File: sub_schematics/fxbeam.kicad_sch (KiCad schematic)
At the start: 16 parts

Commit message: buck converter changes
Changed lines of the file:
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@@
 		(color 0 0 0 0)
 	)
-	(junction
-		(at 49.53 111.76)
-		(diameter 0)
-		(color 0 0 0 0)
-	)
 	(bus_entry
 		(at 109.22 135.89)
@@
 	(wire
 		(pts
-			(xy 46.99 111.76) (xy 49.53 111.76)
+			(xy 46.99 111.76) (xy 52.07 111.76)
 		)
 		(stroke
@@
 		)
 	)
-	(wire
-		(pts
-			(xy 49.53 111.76) (xy 52.07 111.76)
-		)
-		(stroke
-			(width 0)
-			(type default)
-		)
-	)
 	(bus
 		(pts
@@
 					(unit 1)
 				)
-			)
-		)
-	)
-	(symbol
-		(lib_id "power:GND")
-		(at 49.53 111.76 0)
-		(unit 1)
-		(body_style 1)
-		(exclude_from_sim no)
-		(in_bom yes)
-		(on_board yes)
-		(in_pos_files yes)
-		(dnp no)
-		(fields_autoplaced yes)
-		(property "Reference" "#PWR01"
-			(at 49.53 118.11 0)
-			(hide yes)
-			(show_name no)
-			(do_not_autoplace no)
-			(effects
-				(font
-					(size 1.27 1.27)
-				)
-			)
-		)
-		(property "Value" "GND"
-			(at 49.53 116.84 0)
-			(show_name no)
-			(do_not_autoplace no)
-			(effects
-				(font
-					(size 1.27 1.27)
-				)
-			)
-		)
-		(property "Footprint" ""
-			(at 49.53 111.76 0)
-			(hide yes)
-			(show_name no)
-			(do_not_autoplace no)
-			(effects
-				(font
-					(size 1.27 1.27)
-				)
-			)
-		)
-		(property "Datasheet" ""
-			(at 49.53 111.76 0)
-			(hide yes)
-			(show_name no)
-			(do_not_autoplace no)
-			(effects
-				(font
-					(size 1.27 1.27)
-				)
-			)
-		)
-		(property "Description" "Power symbol creates a global label with name \"GND\" , ground"
-			(at 49.53 111.76 0)
-			(hide yes)
-			(show_name no)
-			(do_not_autoplace no)
-			(effects
-				(font
-					(size 1.27 1.27)
-				)
-			)
-		)
-		(pin "1"
-		)
-		(instances
-			(project "fw16_MCIO8i"
-				(path "/50f5fd03-67f8-43d1-8bfe-dca2cf908bf0/8477da45-41b5-48a1-9c5b-2402988eb1f4"
-					(reference "#PWR01")
-					(unit 1)
-				)

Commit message: buck converter component
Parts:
- removed R1: 1206_R_560112132036, resistors:R_Wurth_WRIS-RSKS-1206_R, symbol resistor:1206_R_560112132036
- added R19: 1206_R_560112132036, resistors:R_Wurth_WRIS-RSKS-1206_R, symbol resistor:1206_R_560112132036
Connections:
- net GND: now also R19.2
- net at IN1.SL2 (ID1): now also R19.1

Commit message: Schematics revamped
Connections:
- net PEX_RST renamed PEX.RST

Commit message: Footprint
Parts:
- removed D3, D6: ES15DLW, fan-diode:SODFL3718X102N, symbol fan-diode:ES15DLW
- removed R10, R7, R8, R9: 1206_R_560112132007, resistors:R_Wurth_WRIS-RSKS-1206_R, symbol resistor:1206_R_560112132007
- removed R19, R2: 1206_R_560112132036, resistors:R_Wurth_WRIS-RSKS-1206_R, symbol resistor:1206_R_560112132036
- added R10, R7, R8, R9: 0402_560112110001, WE_WRIS-RSKS:R_Wurth_WRIS-RSKS-0402, symbol WE_WRIS-RSKS:0402_560112110001
- added R19, R2: 0402_560112110088, WE_WRIS-RSKS:R_Wurth_WRIS-RSKS-0402, symbol WE_WRIS-RSKS:0402_560112110088
- R3, R4, R5, R6: value 1206_R_560112132007 -> 0402_560112110001; footprint resistors:R_Wurth_WRIS-RSKS-1206_R -> WE_WRIS-RSKS:R_Wurth_WRIS-RSKS-0402; symbol resistor:1206_R_560112132007 -> WE_WRIS-RSKS:0402_560112110001; H (mm) 0.6 -> 0.35; L (mm) 3.1 -> 1.0; LCSC Part # C25268462 -> (none); MPN 560112132007 -> (none); PRated (mW) 250.0 -> 62.5; Part Number 560112132007 -> 560112110001; Size 1206_R -> 0402; W (mm) 1.6 -> 0.5
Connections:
- net 12V_PWR: now also R7.2
- net FAN1.PWM: now also R9.2
- net FAN1.SPD: now also R8.2
- net GND: now also R6.2, R10.2, R19.1, R2.1
- net at IN1.SL2 (ID1): now also R2.2
- net at IN1.PJ1 (ID0): now also R19.2
- net at FAN_R1.4: now also R7.1
- net at FAN_R1.1: now also R10.1
- net at FAN_R1.3: now also R8.1
- net at FAN_R1.2: now also R9.1

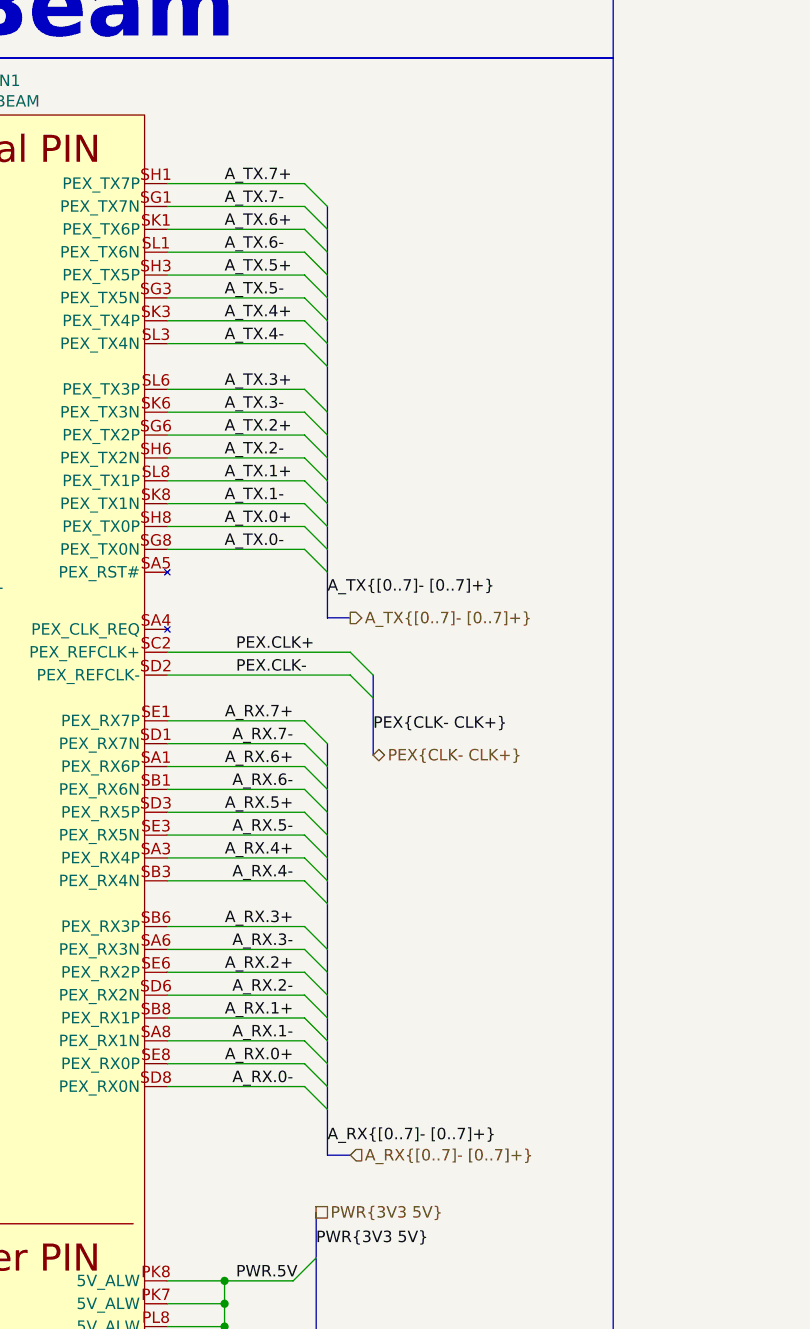
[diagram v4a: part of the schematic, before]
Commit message: PCIe shematic fix
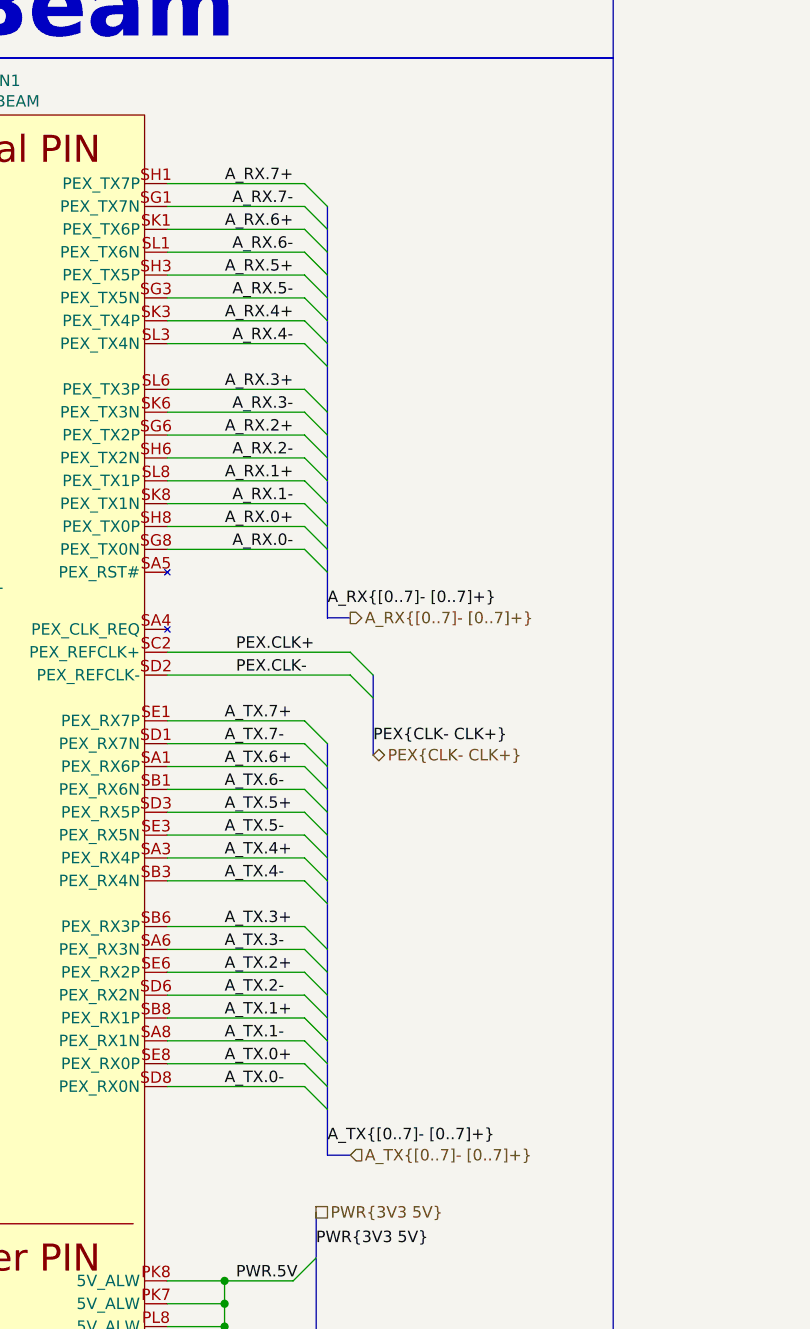
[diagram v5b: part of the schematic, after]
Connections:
- net A_RX.0+: now also IN1.SH8 (PEX_TX0P); no longer IN1.SE8 (PEX_RX0P)
- net A_RX.0-: now also IN1.SG8 (PEX_TX0N); no longer IN1.SD8 (PEX_RX0N)
- net A_RX.1+: now also IN1.SL8 (PEX_TX1P); no longer IN1.SB8 (PEX_RX1P)
- net A_RX.1-: now also IN1.SK8 (PEX_TX1N); no longer IN1.SA8 (PEX_RX1N)
- net A_RX.2+: now also IN1.SG6 (PEX_TX2P); no longer IN1.SE6 (PEX_RX2P)
- net A_RX.2-: now also IN1.SH6 (PEX_TX2N); no longer IN1.SD6 (PEX_RX2N)
- net A_RX.3+: now also IN1.SL6 (PEX_TX3P); no longer IN1.SB6 (PEX_RX3P)
- net A_RX.3-: now also IN1.SK6 (PEX_TX3N); no longer IN1.SA6 (PEX_RX3N)
- net A_RX.4+: now also IN1.SK3 (PEX_TX4P); no longer IN1.SA3 (PEX_RX4P)
- net A_RX.4-: now also IN1.SL3 (PEX_TX4N); no longer IN1.SB3 (PEX_RX4N)
- net A_RX.5+: now also IN1.SH3 (PEX_TX5P); no longer IN1.SD3 (PEX_RX5P)
- net A_RX.5-: now also IN1.SG3 (PEX_TX5N); no longer IN1.SE3 (PEX_RX5N)
- net A_RX.6+: now also IN1.SK1 (PEX_TX6P); no longer IN1.SA1 (PEX_RX6P)
- net A_RX.6-: now also IN1.SL1 (PEX_TX6N); no longer IN1.SB1 (PEX_RX6N)
- net A_RX.7+: now also IN1.SH1 (PEX_TX7P); no longer IN1.SE1 (PEX_RX7P)
- net A_RX.7-: now also IN1.SG1 (PEX_TX7N); no longer IN1.SD1 (PEX_RX7N)
- net A_TX.0+: now also IN1.SE8 (PEX_RX0P); no longer IN1.SH8 (PEX_TX0P)
- net A_TX.0-: now also IN1.SD8 (PEX_RX0N); no longer IN1.SG8 (PEX_TX0N)
- net A_TX.1+: now also IN1.SB8 (PEX_RX1P); no longer IN1.SL8 (PEX_TX1P)
- net A_TX.1-: now also IN1.SA8 (PEX_RX1N); no longer IN1.SK8 (PEX_TX1N)
- net A_TX.2+: now also IN1.SE6 (PEX_RX2P); no longer IN1.SG6 (PEX_TX2P)
- net A_TX.2-: now also IN1.SD6 (PEX_RX2N); no longer IN1.SH6 (PEX_TX2N)
- net A_TX.3+: now also IN1.SB6 (PEX_RX3P); no longer IN1.SL6 (PEX_TX3P)
- net A_TX.3-: now also IN1.SA6 (PEX_RX3N); no longer IN1.SK6 (PEX_TX3N)
- net A_TX.4+: now also IN1.SA3 (PEX_RX4P); no longer IN1.SK3 (PEX_TX4P)
- net A_TX.4-: now also IN1.SB3 (PEX_RX4N); no longer IN1.SL3 (PEX_TX4N)
- net A_TX.5+: now also IN1.SD3 (PEX_RX5P); no longer IN1.SH3 (PEX_TX5P)
- net A_TX.5-: now also IN1.SE3 (PEX_RX5N); no longer IN1.SG3 (PEX_TX5N)
- net A_TX.6+: now also IN1.SA1 (PEX_RX6P); no longer IN1.SK1 (PEX_TX6P)
- net A_TX.6-: now also IN1.SB1 (PEX_RX6N); no longer IN1.SL1 (PEX_TX6N)
- net A_TX.7+: now also IN1.SE1 (PEX_RX7P); no longer IN1.SH1 (PEX_TX7P)
- net A_TX.7-: now also IN1.SD1 (PEX_RX7N); no longer IN1.SG1 (PEX_TX7N)

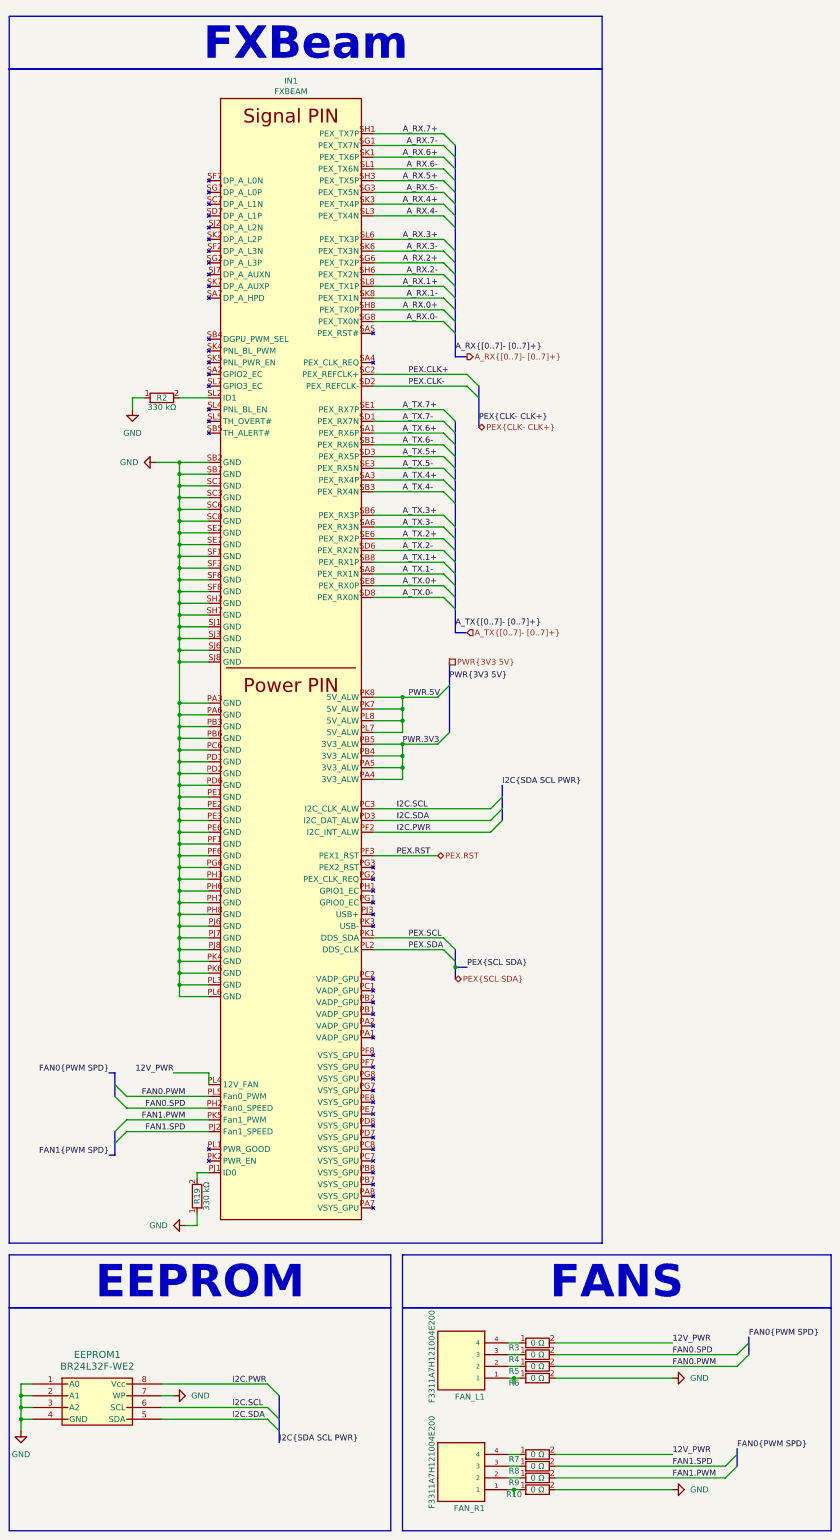
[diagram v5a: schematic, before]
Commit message: Switch to retimer for only clock
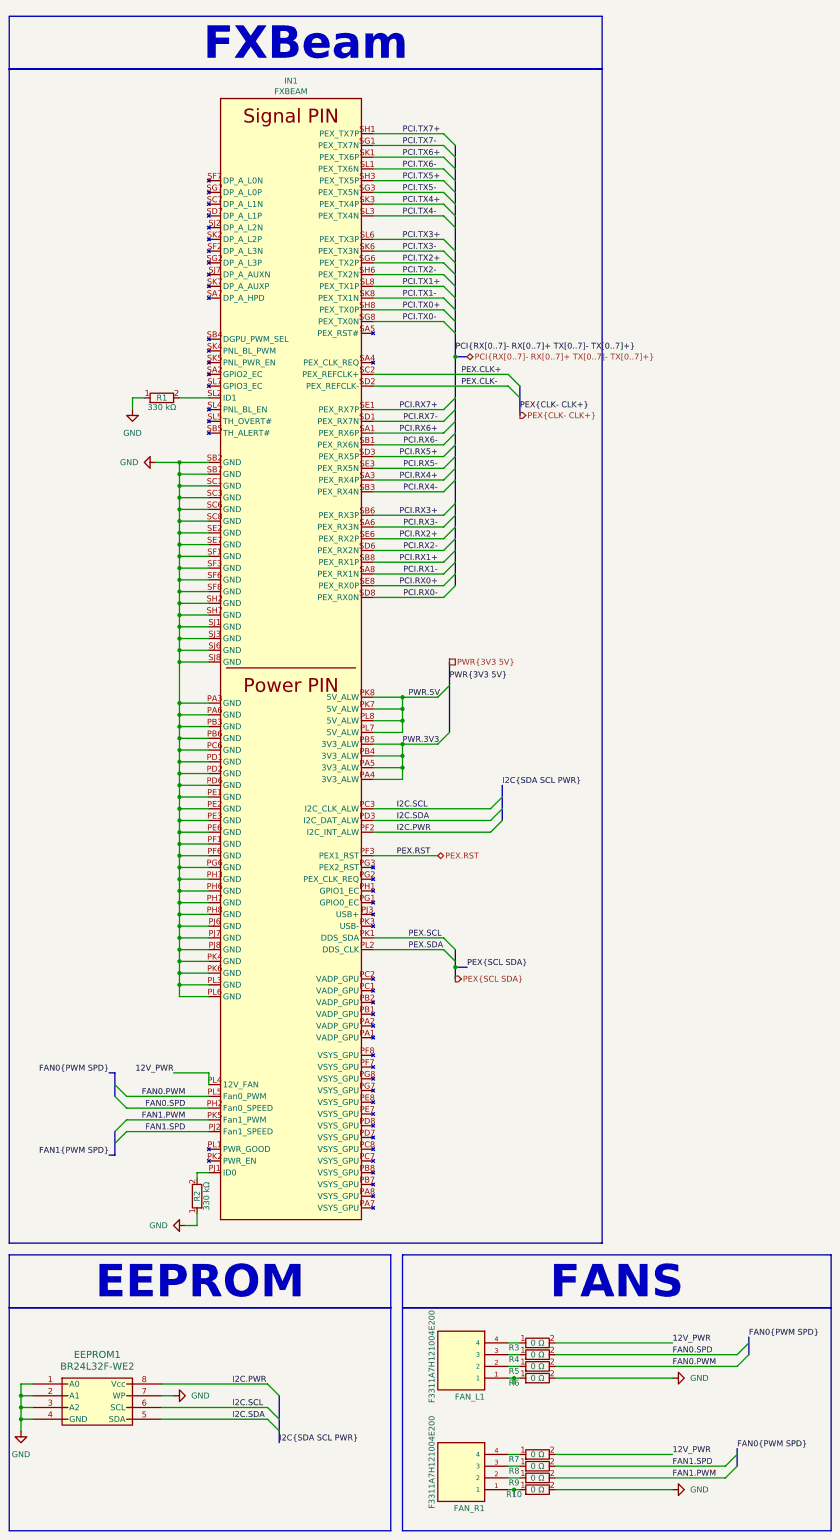
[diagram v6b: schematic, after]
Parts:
- renumbered R2 to R1, R19 to R2
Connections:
- net A_RX.0+ renamed PCI.TX0+
- net A_RX.0- renamed PCI.TX0-
- net A_RX.1+ renamed PCI.TX1+
- net A_RX.1- renamed PCI.TX1-
- net A_RX.2+ renamed PCI.TX2+
- net A_RX.2- renamed PCI.TX2-
- net A_RX.3+ renamed PCI.TX3+
- net A_RX.3- renamed PCI.TX3-
- net A_RX.4+ renamed PCI.TX4+
- net A_RX.4- renamed PCI.TX4-
- net A_RX.5+ renamed PCI.TX5+
- net A_RX.5- renamed PCI.TX5-
- net A_RX.6+ renamed PCI.TX6+
- net A_RX.6- renamed PCI.TX6-
- net A_RX.7+ renamed PCI.TX7+
- net A_RX.7- renamed PCI.TX7-
- net A_TX.0+ renamed PCI.RX0+
- net A_TX.0- renamed PCI.RX0-
- net A_TX.1+ renamed PCI.RX1+
- net A_TX.1- renamed PCI.RX1-
- net A_TX.2+ renamed PCI.RX2+
- net A_TX.2- renamed PCI.RX2-
- net A_TX.3+ renamed PCI.RX3+
- net A_TX.3- renamed PCI.RX3-
- net A_TX.4+ renamed PCI.RX4+
- net A_TX.4- renamed PCI.RX4-
- net A_TX.5+ renamed PCI.RX5+
- net A_TX.5- renamed PCI.RX5-
- net A_TX.6+ renamed PCI.RX6+
- net A_TX.6- renamed PCI.RX6-
- net A_TX.7+ renamed PCI.RX7+
- net A_TX.7- renamed PCI.RX7-

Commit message: Fixed board dimensions
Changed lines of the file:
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@@
 	)
 	(junction
-		(at 111.76 88.9)
+		(at 52.07 134.62)
 		(diameter 0)
 		(color 0 0 0 0)
 	)
 	(junction
-		(at 52.07 134.62)
+		(at 52.07 147.32)
 		(diameter 0)
 		(color 0 0 0 0)
 	)
 	(junction
-		(at 52.07 147.32)
+		(at 111.76 88.9)
 		(diameter 0)
 		(color 0 0 0 0)
@@
 		)
 	)
+	(bus
+		(pts
+			(xy 111.76 88.9) (xy 118.11 88.9)
+		)
+		(stroke
+			(width 0)
+			(type default)
+		)
+	)
 	(wire
 		(pts
@@
 		)
 	)
-	(bus
-		(pts
-			(xy 111.76 88.9) (xy 111.76 97.79)
-		)
-		(stroke
-			(width 0)
-			(type default)
-		)
-	)
 	(wire
 		(pts
@@
 	(bus
 		(pts
+			(xy 111.76 88.9) (xy 111.76 97.79)
+		)
+		(stroke
+			(width 0)
+			(type default)
+		)
+	)
+	(bus
+		(pts
 			(xy 111.76 133.35) (xy 111.76 130.81)
 		)
@@
 		)
 	)
-	(bus
-		(pts
-			(xy 111.76 88.9) (xy 114.3 88.9)
-		)
-		(stroke
-			(width 0)
-			(type default)
-		)
-	)
 	(wire
 		(pts
@@
 		)
 	)
+	(label "PCI{RX[0..7]- RX[0..7]+ TX[0..7]- TX[0..7]+}"
+		(at 116.84 88.9 90)
+		(effects
+			(font
+				(size 1.27 1.27)
+			)
+			(justify left bottom)
+		)
+	)
 	(label "I2C{SDA SCL PWR}"
 		(at 73.66 323.85 0)
@@
 		)
 	)
-	(label "PCI{RX[0..7]- RX[0..7]+ TX[0..7]- TX[0..7]+}"
-		(at 111.76 87.63 0)
-		(effects
-			(font
-				(size 1.27 1.27)
-			)
-			(justify left bottom)
-		)
-	)
 	(label "PCI.RX1-"
 		(at 107.95 135.89 180)
@@
 	(hierarchical_label "PCI{RX[0..7]- RX[0..7]+ TX[0..7]- TX[0..7]+}"
 		(shape bidirectional)
-		(at 114.3 88.9 0)
+		(at 118.11 88.9 90)
 		(effects
 			(font

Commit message: Preparing order
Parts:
- R1, R2: MPN (none) -> 560112110088
- R10, R3, R4, R5, R6, R7, R8, R9: JLCPCB Part # (none) -> C22463254; MPN (none) -> 560112110001
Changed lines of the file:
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@@
 			)
 		)
+		(property "MPN" "560112110001"
+			(at 129.54 331.47 0)
+			(hide yes)
+			(show_name no)
+			(do_not_autoplace no)
+			(effects
+				(font
+					(size 1.27 1.27)
+				)
+			)
+		)
+		(property "JLCPCB Part #" "C22463254"
+			(at 129.54 331.47 0)
+			(hide yes)
+			(show_name no)
+			(do_not_autoplace no)
+			(effects
+				(font
+					(size 1.27 1.27)
+				)
+			)
+		)
 		(pin "2"
 		)
@@
 			)
 		)
+		(property "MPN" "560112110001"
+			(at 129.54 302.26 0)
+			(hide yes)
+			(show_name no)
+			(do_not_autoplace no)
+			(effects
+				(font
+					(size 1.27 1.27)
+				)
+			)
+		)
+		(property "JLCPCB Part #" "C22463254"
+			(at 129.54 302.26 0)
+			(hide yes)
+			(show_name no)
+			(do_not_autoplace no)
+			(effects
+				(font
+					(size 1.27 1.27)
+				)
+			)
+		)
 		(pin "2"
 		)
@@
 			)
 		)
+		(property "MPN" "560112110001"
+			(at 129.54 328.93 0)
+			(hide yes)
+			(show_name no)
+			(do_not_autoplace no)
+			(effects
+				(font
+					(size 1.27 1.27)
+				)
+			)
+		)
+		(property "JLCPCB Part #" "C22463254"
+			(at 129.54 328.93 0)
+			(hide yes)
+			(show_name no)
+			(do_not_autoplace no)
+			(effects
+				(font
+					(size 1.27 1.27)
+				)
+			)
+		)
 		(pin "2"
 		)
@@
 			)
 		)
+		(property "MPN" "560112110001"
+			(at 129.54 304.8 0)
+			(hide yes)
+			(show_name no)
+			(do_not_autoplace no)
+			(effects
+				(font
+					(size 1.27 1.27)
+				)
+			)
+		)
+		(property "JLCPCB Part #" "C22463254"
+			(at 129.54 304.8 0)
+			(hide yes)
+			(show_name no)
+			(do_not_autoplace no)
+			(effects
+				(font
+					(size 1.27 1.27)
+				)
+			)
+		)
 		(pin "2"
 		)
@@
 			)
 		)
+		(property "MPN" "560112110088"
+			(at 55.88 270.51 0)
+			(hide yes)
+			(show_name no)
+			(do_not_autoplace no)
+			(effects
+				(font
+					(size 1.27 1.27)
+				)
+			)
+		)
 		(pin "1"
 		)
@@
 			)
 		)
+		(property "MPN" "560112110001"
+			(at 129.54 334.01 0)
+			(hide yes)
+			(show_name no)
+			(do_not_autoplace no)
+			(effects
+				(font
+					(size 1.27 1.27)
+				)
+			)
+		)
+		(property "JLCPCB Part #" "C22463254"
+			(at 129.54 334.01 0)
+			(hide yes)
+			(show_name no)
+			(do_not_autoplace no)
+			(effects
+				(font
+					(size 1.27 1.27)
+				)
+			)
+		)
 		(pin "2"
 		)
@@
 			)
 		)
+		(property "MPN" "560112110001"
+			(at 129.54 309.88 0)
+			(hide yes)
+			(show_name no)
+			(do_not_autoplace no)
+			(effects
+				(font
+					(size 1.27 1.27)
+				)
+			)
+		)
+		(property "JLCPCB Part #" "C22463254"
+			(at 129.54 309.88 0)
+			(hide yes)
+			(show_name no)
+			(do_not_autoplace no)
+			(effects
+				(font
+					(size 1.27 1.27)
+				)
+			)
+		)
 		(pin "2"
 		)
@@
 			)
 		)
+		(property "MPN" "560112110088"
+			(at 48.26 97.79 0)
+			(hide yes)
+			(show_name no)
+			(do_not_autoplace no)
+			(effects
+				(font
+					(size 1.27 1.27)
+				)
+			)
+		)
 		(pin "1"
 		)
@@
 			)
 		)
+		(property "MPN" "560112110001"
+			(at 129.54 326.39 0)
+			(hide yes)
+			(show_name no)
+			(do_not_autoplace no)
+			(effects
+				(font
+					(size 1.27 1.27)
+				)
+			)
+		)
+		(property "JLCPCB Part #" "C22463254"
+			(at 129.54 326.39 0)
+			(hide yes)
+			(show_name no)
+			(do_not_autoplace no)
+			(effects
+				(font
+					(size 1.27 1.27)
+				)
+			)
+		)
 		(pin "2"
 		)
@@
 			(effects
 				(font
+					(size 1.27 1.27)
+				)
+			)
+		)
+		(property "MPN" "560112110001"
+			(at 129.54 307.34 0)
+			(hide yes)
+			(show_name no)
+			(do_not_autoplace no)
+			(effects
+				(font
+					(size 1.27 1.27)
+				)
+			)
+		)
+		(property "JLCPCB Part #" "C22463254"
+			(at 129.54 307.34 0)
+			(hide yes)
+			(show_name no)
+			(do_not_autoplace no)
+			(effects
+				(font
